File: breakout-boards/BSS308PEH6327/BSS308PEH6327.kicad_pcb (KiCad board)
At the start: 2 copper layers, 15 parts, among them J1 Conn_01x12, J2 Conn_01x12, J3 Conn_01x12, Q1 BSS308PE_H6327, Q10 BSS308PE_H6327, Q11 BSS308PE_H6327, Q12 BSS308PE_H6327, Q2 BSS308PE_H6327, Q3 BSS308PE_H6327, Q4 BSS308PE_H6327, Q5 BSS308PE_H6327, Q6 BSS308PE_H6327, Q7 BSS308PE_H6327, Q8 BSS308PE_H6327, Q9 BSS308PE_H6327

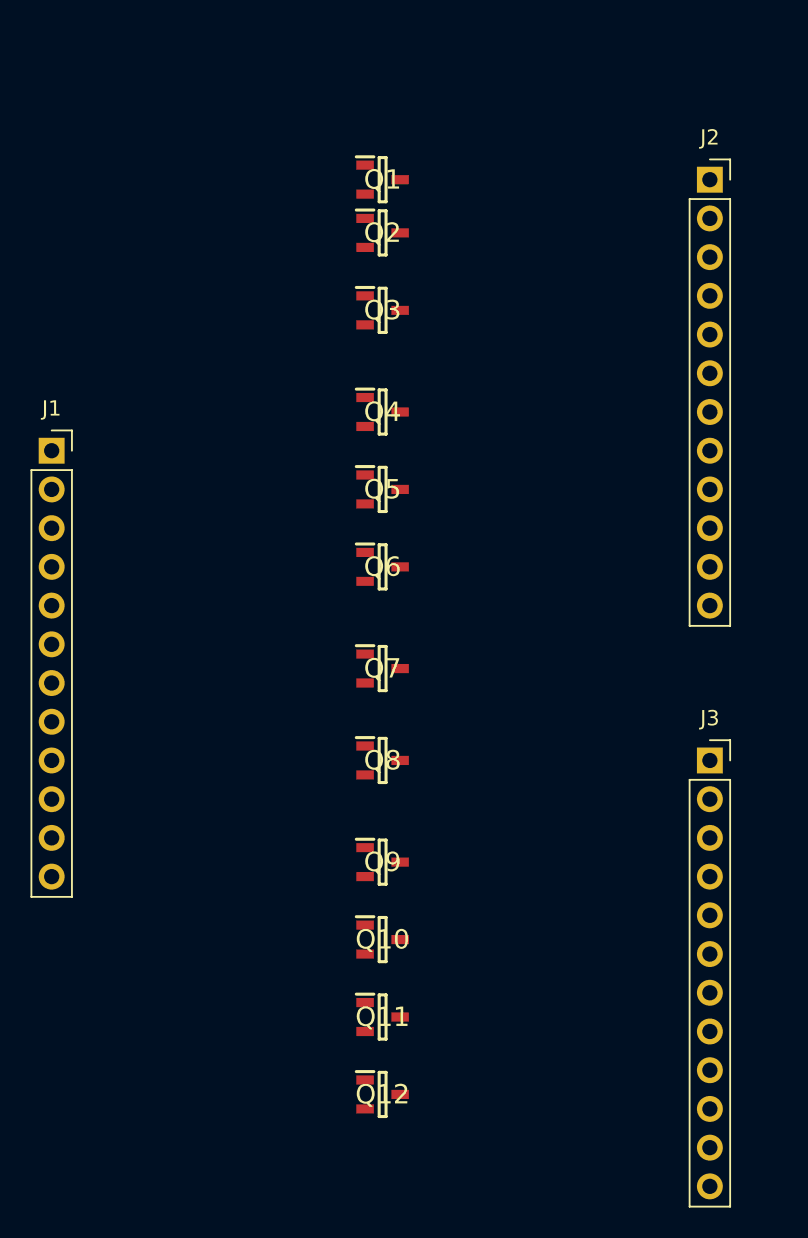
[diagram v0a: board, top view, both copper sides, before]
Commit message: feat: update MOSFET pcb and schem
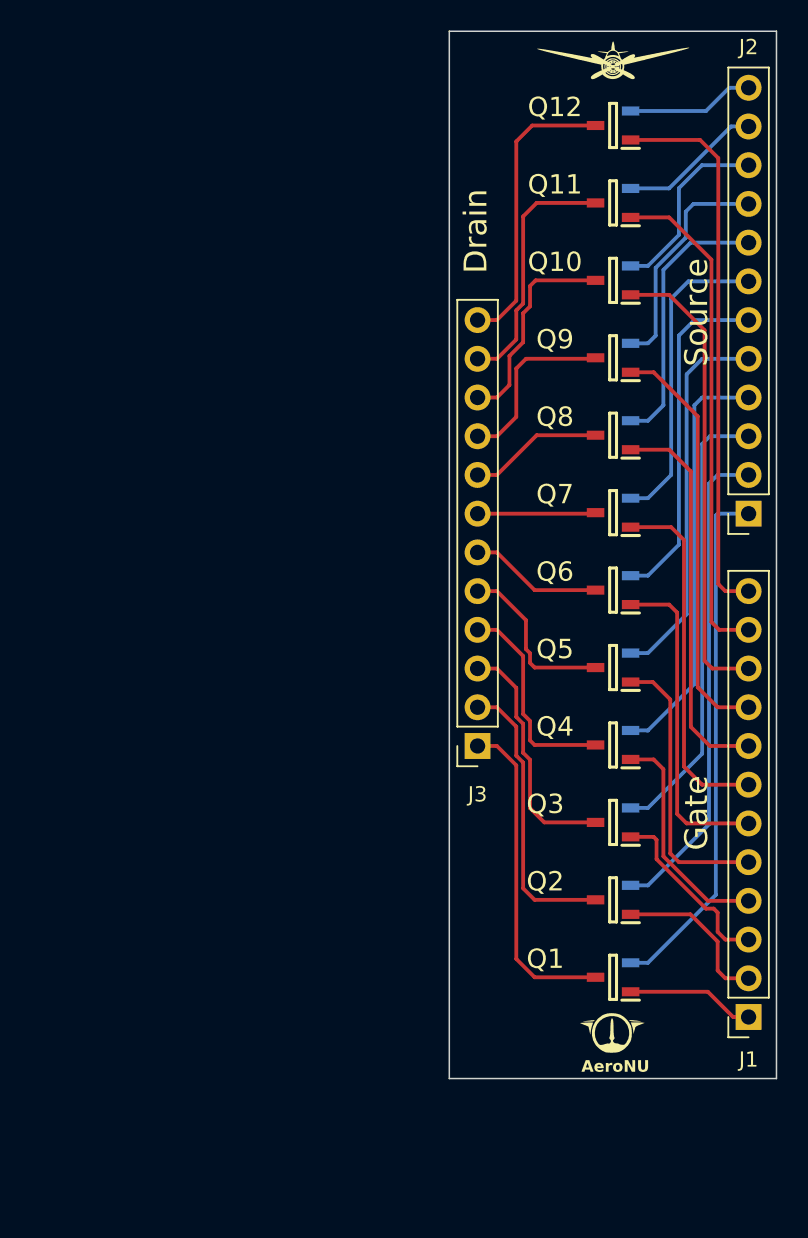
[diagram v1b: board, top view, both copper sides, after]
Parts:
- added AeroNU: LOGO, FixedWing:AeroNU - Logo (Smol), F.Cu at (161.4, 115.6)
- added FixedWing: LOGO, FixedWing:FixedWing - Logo (Smol), F.Cu at (161.3, 49.7)
- moved J1 58.9 mm to (170.2, 111.8), turned to 180 degrees
- moved J2 22.1 mm to (170.2, 78.7), turned to 180 degrees
- moved Q1 17.0 mm to (161.3, 109.2), turned to 180 degrees
- moved Q2 17.0 mm to (161.3, 104.1), turned to 180 degrees
- moved Q3 17.0 mm to (161.3, 99.0), turned to 180 degrees
- moved Q4 17.0 mm to (161.3, 93.9), turned to 180 degrees
- moved Q5 16.3 mm to (161.3, 88.8), turned to 180 degrees
- moved Q6 16.0 mm to (161.3, 83.8), turned to 180 degrees
- moved Q8 15.5 mm to (161.3, 73.6), turned to 180 degrees
- moved Q12 15.5 mm to (161.3, 53.3), turned to 180 degrees
- moved Q7 15.5 mm to (161.3, 78.7), turned to 180 degrees
- moved Q9 15.5 mm to (161.3, 68.5), turned to 180 degrees
- moved J3 15.3 mm to (152.4, 94.0), turned to 180 degrees
- moved Q10 15.2 mm to (161.3, 63.4), turned to 180 degrees
- moved Q11 15.2 mm to (161.3, 58.4), turned to 180 degrees
- renumbered Q12 to Q1, Q3 to Q10, Q2 to Q11, Q1 to Q12, Q11 to Q2, Q10 to Q3, Q9 to Q4, Q8 to Q5, Q7 to Q6, Q6 to Q7, Q5 to Q8, Q4 to Q9
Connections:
- J1 pad 1: Net-(J1-Pin_1) -> (no net)
- J1 pad 10: Net-(J1-Pin_10) -> (no net)
- J1 pad 11: Net-(J1-Pin_11) -> (no net)
- J1 pad 12: Net-(J1-Pin_12) -> (no net)
- J1 pad 2: Net-(J1-Pin_2) -> (no net)
- J1 pad 3: Net-(J1-Pin_3) -> (no net)
- J1 pad 4: Net-(J1-Pin_4) -> (no net)
- J1 pad 5: Net-(J1-Pin_5) -> (no net)
- J1 pad 6: Net-(J1-Pin_6) -> (no net)
- J1 pad 7: Net-(J1-Pin_7) -> (no net)
- J1 pad 8: Net-(J1-Pin_8) -> (no net)
- J1 pad 9: Net-(J1-Pin_9) -> (no net)
- J2 pad 1: Net-(J2-Pin_1) -> (no net)
- J2 pad 10: Net-(J2-Pin_10) -> (no net)
- J2 pad 11: Net-(J2-Pin_11) -> (no net)
- J2 pad 12: Net-(J2-Pin_12) -> (no net)
- J2 pad 2: Net-(J2-Pin_2) -> (no net)
- J2 pad 3: Net-(J2-Pin_3) -> (no net)
- J2 pad 4: Net-(J2-Pin_4) -> (no net)
- J2 pad 5: Net-(J2-Pin_5) -> (no net)
- J2 pad 6: Net-(J2-Pin_6) -> (no net)
- J2 pad 7: Net-(J2-Pin_7) -> (no net)
- J2 pad 8: Net-(J2-Pin_8) -> (no net)
- J2 pad 9: Net-(J2-Pin_9) -> (no net)
- J3 pad 1: Net-(J3-Pin_1) -> (no net)
- J3 pad 10: Net-(J3-Pin_10) -> (no net)
- J3 pad 11: Net-(J3-Pin_11) -> (no net)
- J3 pad 12: Net-(J3-Pin_12) -> (no net)
- J3 pad 2: Net-(J3-Pin_2) -> (no net)
- J3 pad 3: Net-(J3-Pin_3) -> (no net)
- J3 pad 4: Net-(J3-Pin_4) -> (no net)
- J3 pad 5: Net-(J3-Pin_5) -> (no net)
- J3 pad 6: Net-(J3-Pin_6) -> (no net)
- J3 pad 7: Net-(J3-Pin_7) -> (no net)
- J3 pad 8: Net-(J3-Pin_8) -> (no net)
- J3 pad 9: Net-(J3-Pin_9) -> (no net)
- Q1 pad 2: Net-(J3-Pin_12) -> Net-(J2-Pin_12)
- Q1 pad 3: Net-(J2-Pin_12) -> Net-(J3-Pin_12)
- Q10 pad 2: Net-(J3-Pin_3) -> Net-(J2-Pin_3)
- Q10 pad 3: Net-(J2-Pin_3) -> Net-(J3-Pin_3)
- Q11 pad 2: Net-(J3-Pin_2) -> Net-(J2-Pin_2)
- Q11 pad 3: Net-(J2-Pin_2) -> Net-(J3-Pin_2)
- Q12 pad 2: Net-(J3-Pin_1) -> Net-(J2-Pin_1)
- Q12 pad 3: Net-(J2-Pin_1) -> Net-(J3-Pin_1)
- Q2 pad 2: Net-(J3-Pin_11) -> Net-(J2-Pin_11)
- Q2 pad 3: Net-(J2-Pin_11) -> Net-(J3-Pin_11)
- Q3 pad 2: Net-(J3-Pin_10) -> Net-(J2-Pin_10)
- Q3 pad 3: Net-(J2-Pin_10) -> Net-(J3-Pin_10)
- Q4 pad 2: Net-(J3-Pin_9) -> Net-(J2-Pin_9)
- Q4 pad 3: Net-(J2-Pin_9) -> Net-(J3-Pin_9)
- Q5 pad 2: Net-(J3-Pin_8) -> Net-(J2-Pin_8)
- Q5 pad 3: Net-(J2-Pin_8) -> Net-(J3-Pin_8)
- Q6 pad 2: Net-(J3-Pin_7) -> Net-(J2-Pin_7)
- Q6 pad 3: Net-(J2-Pin_7) -> Net-(J3-Pin_7)
- Q7 pad 2: Net-(J3-Pin_6) -> Net-(J2-Pin_6)
- Q7 pad 3: Net-(J2-Pin_6) -> Net-(J3-Pin_6)
- Q8 pad 2: Net-(J3-Pin_5) -> Net-(J2-Pin_5)
- Q8 pad 3: Net-(J2-Pin_5) -> Net-(J3-Pin_5)
- Q9 pad 2: Net-(J3-Pin_4) -> Net-(J2-Pin_4)
- Q9 pad 3: Net-(J2-Pin_4) -> Net-(J3-Pin_4)
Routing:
- net Net-(J1-Pin_1): track 0.00 -> 36.4 mm
- net Net-(J2-Pin_12): track 0.00 -> 34.5 mm
- net Net-(J1-Pin_2): track 0.00 -> 32.9 mm
- net Net-(J2-Pin_11): track 0.00 -> 32.0 mm
- net Net-(J1-Pin_3): track 0.00 -> 30.6 mm
- net Net-(J2-Pin_10): track 0.00 -> 29.7 mm
- net Net-(J2-Pin_9): track 0.00 -> 27.5 mm
- net Net-(J1-Pin_4): track 0.00 -> 27.3 mm
- net Net-(J1-Pin_5): track 0.00 -> 25.6 mm
- net Net-(J2-Pin_8): track 0.00 -> 25.0 mm
- net Net-(J1-Pin_6): track 0.00 -> 23.4 mm
- net Net-(J2-Pin_7): track 0.00 -> 22.7 mm
- net Net-(J3-Pin_12): track 0.00 -> 21.5 mm
- net Net-(J1-Pin_7): track 0.00 -> 21.4 mm
- net Net-(J2-Pin_6): track 0.00 -> 20.4 mm
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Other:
- board outline added: 21.5 x 68.7 mm
- board text added: "AeroNU"
- board text added: "Designed By Ephram CJ and Matthew F"
- board text added: "Drain"
- board text added: "Gate"
- board text added: "Source"

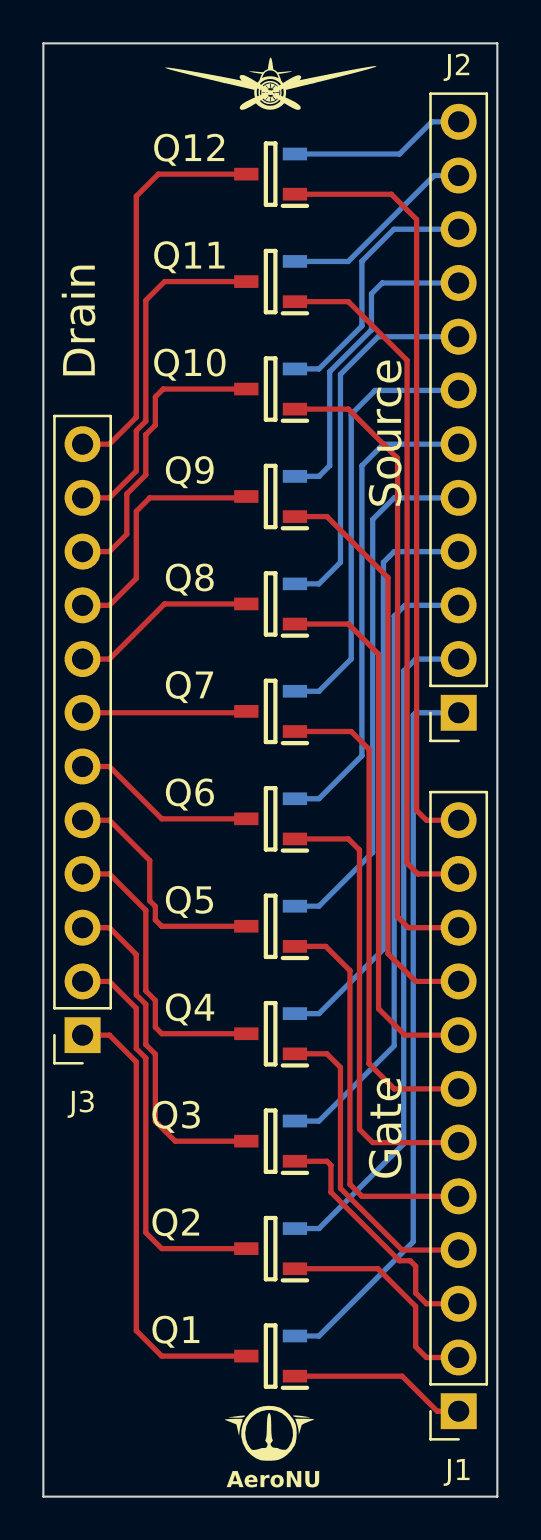
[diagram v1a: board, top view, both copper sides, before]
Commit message: feat: change fixed wing logo and component positioning
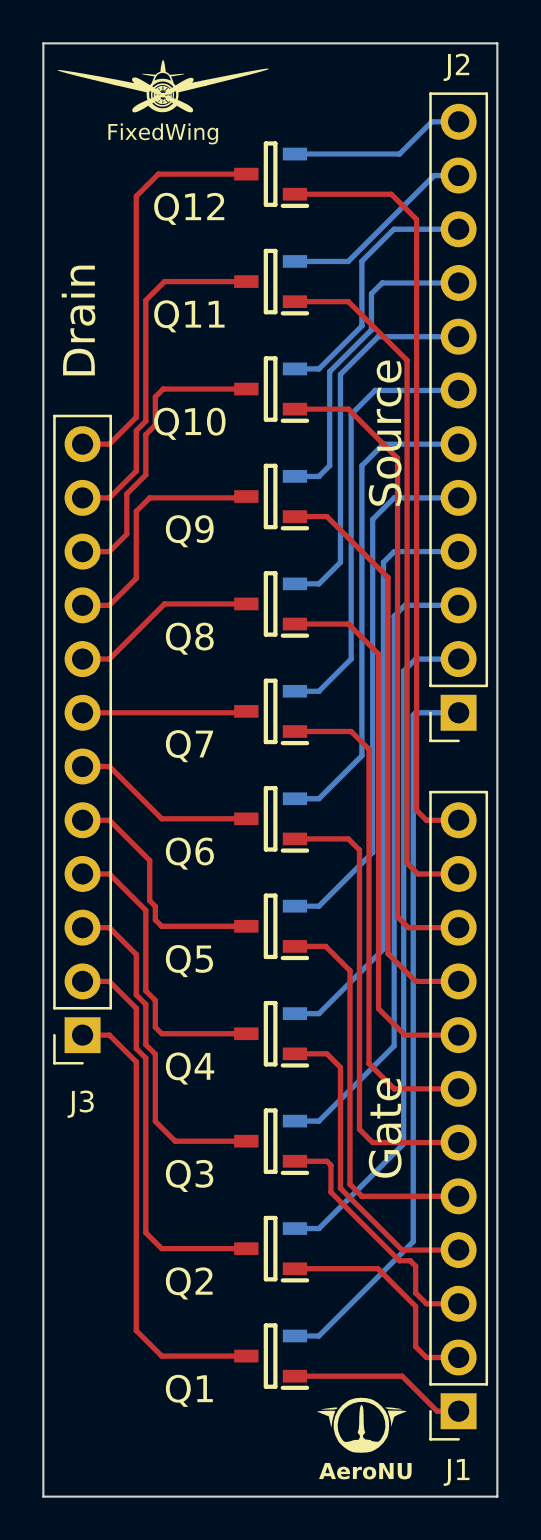
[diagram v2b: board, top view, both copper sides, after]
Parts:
- moved FixedWing 5.10 mm to (156.2, 49.5)
- moved AeroNU 4.39 mm to (165.7, 115.2)

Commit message: feat: add fillets to all boards
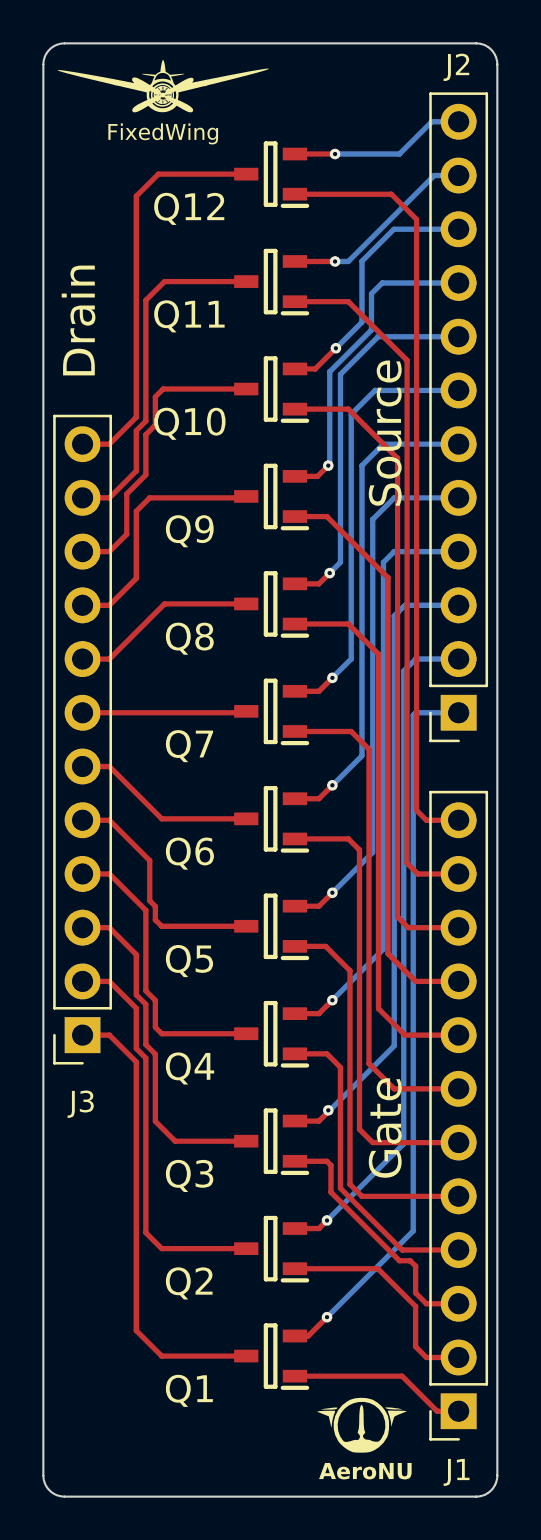
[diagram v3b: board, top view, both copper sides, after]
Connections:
- J2 pad 1: (no net) -> Net-(J2-Pin_12)
- J2 pad 10: (no net) -> Net-(J2-Pin_3)
- J2 pad 8: (no net) -> Net-(J2-Pin_5)
- J2 pad 9: (no net) -> Net-(J2-Pin_4)
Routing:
- net Net-(J2-Pin_12): track 34.5 -> 34.2 mm, vias 0 -> 1
- net Net-(J2-Pin_3): track 12.3 -> 12.2 mm, vias 0 -> 1
- net Net-(J2-Pin_4): vias 0 -> 1
- net Net-(J2-Pin_10): track 29.7 -> 29.8 mm, vias 0 -> 1
- net Net-(J2-Pin_9): vias 0 -> 1
- net Net-(J2-Pin_6): vias 0 -> 1
- net Net-(J2-Pin_8): vias 0 -> 1
- net Net-(J2-Pin_7): vias 0 -> 1
- net Net-(J2-Pin_5): vias 0 -> 1
- net Net-(J2-Pin_2): vias 0 -> 1
- net Net-(J2-Pin_11): vias 0 -> 1
- net Net-(J2-Pin_1): vias 0 -> 1
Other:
- outline, holes or cut-outs redrawn
